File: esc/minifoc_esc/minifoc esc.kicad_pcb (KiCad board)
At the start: 4 copper layers, 31.6 x 23.8 mm, 47 parts, among them J2 Conn_01x03, J4 USB_C_Receptacle_USB2.0_16P, SW1 RESET, SW2 BOOT, U1 DRV8316CRRGFR, U2 RP2040, U3 W25Q64JVXGIQ TR, Y1 12Mhz

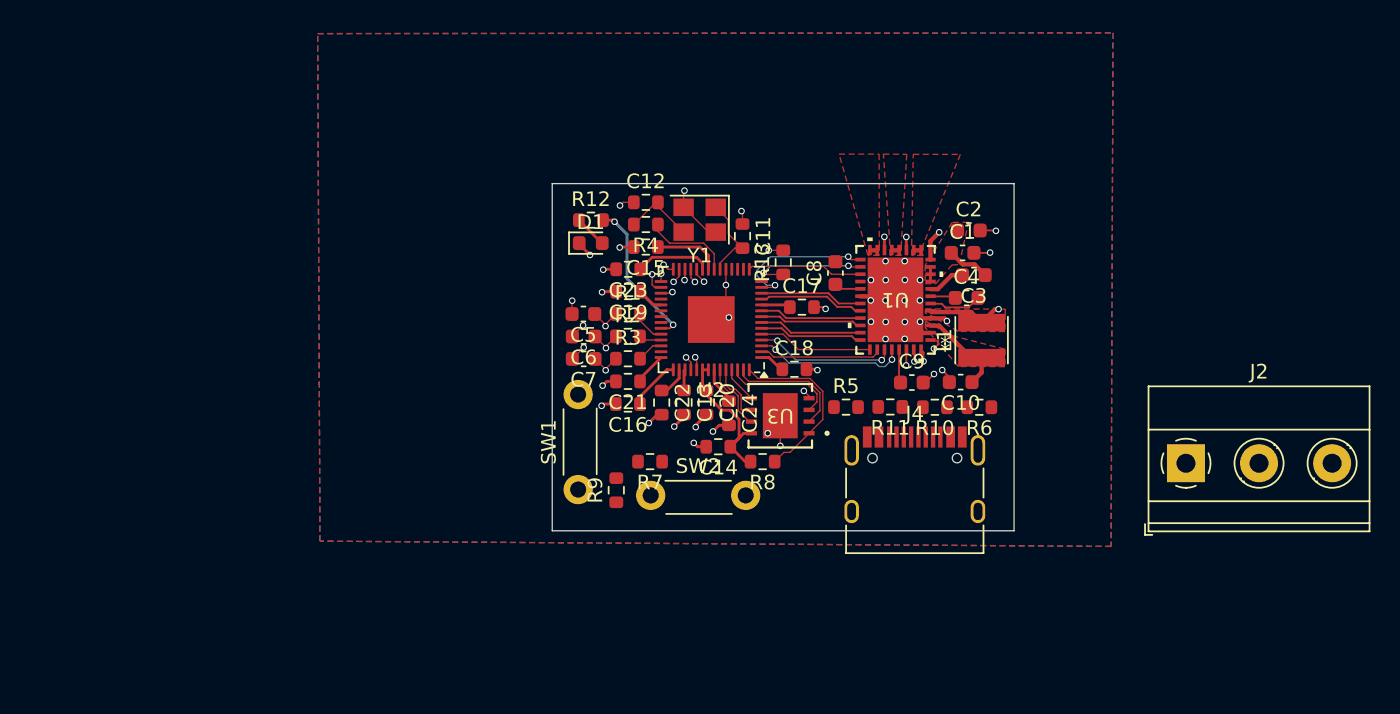
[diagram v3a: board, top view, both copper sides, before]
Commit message: Feat[minifoc_esc]: draft PCB
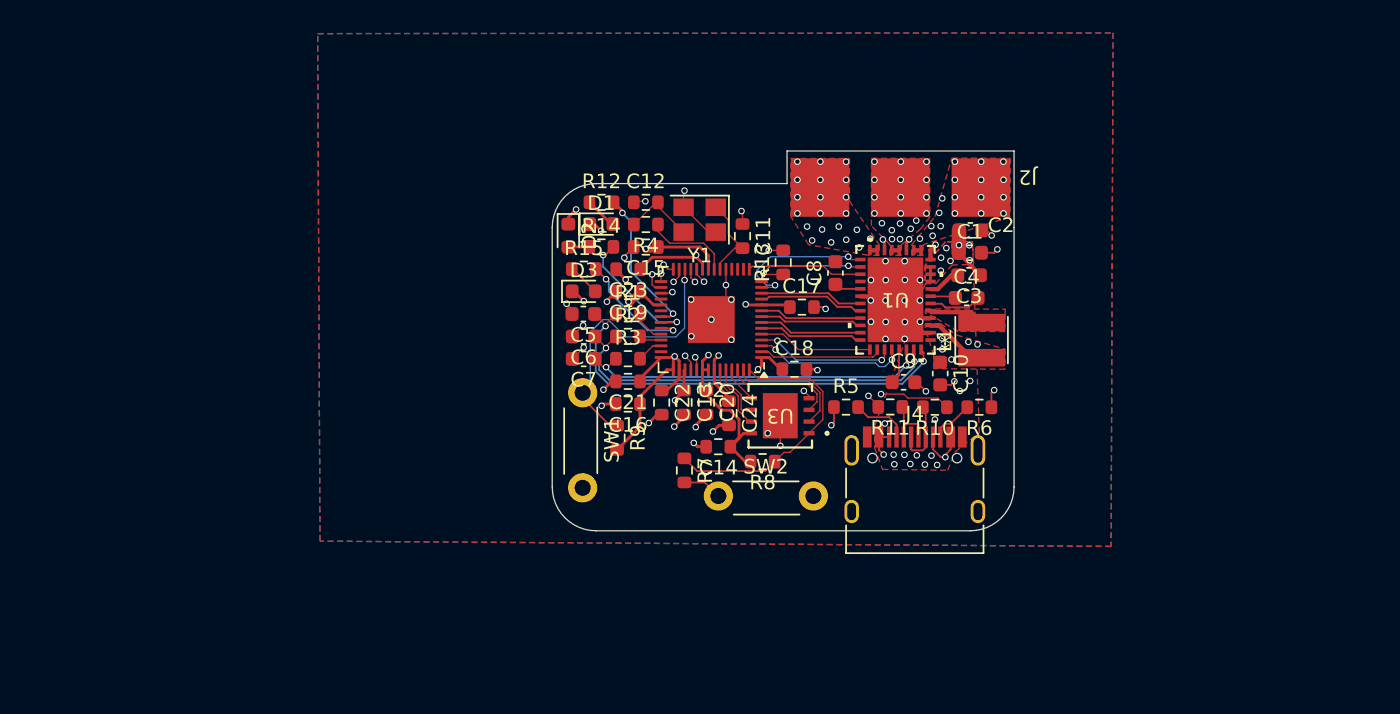
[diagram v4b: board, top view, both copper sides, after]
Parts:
- added D2: LED_Small, LED_SMD:LED_0603_1608Metric, F.Cu at (144.3, 104.0)
- added D3: LED_Small, LED_SMD:LED_0603_1608Metric, F.Cu at (145.4, 107.8)
- added R14: 2.7k, Resistor_SMD:R_0603_1608Metric, F.Cu at (146.6, 104.8)
- added R15: 2.7k, Resistor_SMD:R_0603_1608Metric, F.Cu at (145.4, 106.3)
- J2: footprint TerminalBlock_Phoenix:TerminalBlock_Phoenix_MKDS-1,5-3_1x03_P5.00mm_Horizontal -> DRV8316C:ESC
- moved J2 28.6 mm to (167.0, 98.7), turned to 180 degrees
- moved SW1 6.63 mm to (145.3, 114.8), turned to -90 degrees
- moved SW2 4.63 mm to (154.6, 121.8)
- moved R9 3.59 mm to (147.6, 117.8), turned to -90 degrees
- moved R7 2.43 mm to (152.2, 120.1), turned to -90 degrees
- moved C10 1.52 mm to (169.7, 113.5), turned to -90 degrees
- moved D1 1.49 mm to (146.6, 103.2)
- moved R12 1.42 mm to (146.6, 101.7)
- moved C9 0.57 mm to (167.2, 114.0)
- moved C1 0.51 mm to (171.8, 105.2)
- moved C3 0.33 mm to (171.7, 106.7)
- moved C2 0.10 mm to (171.8, 103.7)
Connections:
- J4 pad A4: /RP2040/VBUS -> VCC
- J4 pad A8: unconnected-(J4-SBU1-PadA8) -> VCC
- J4 pad A9: /RP2040/VBUS -> VCC
- J4 pad B4: /RP2040/VBUS -> VCC
- J4 pad B8: unconnected-(J4-SBU2-PadB8) -> VCC
- J4 pad B9: /RP2040/VBUS -> VCC
- R1 pad 2: /SOA -> /RP2040/SA
- R12 pad 2: /RP2040/LED -> /RP2040/LED3
- R2 pad 2: /SOB -> /RP2040/SB
- R3 pad 2: /SOC -> /RP2040/SC
- U2 pad 35: unconnected-(U2-GPIO23-Pad35) -> /RP2040/LED3
- U2 pad 36: unconnected-(U2-GPIO24-Pad36) -> /RP2040/LED2
- U2 pad 37: /RP2040/LED -> /RP2040/LED1
- U2 pad 38: /SOA -> /RP2040/SA
- U2 pad 39: /SOB -> /RP2040/SB
- U2 pad 40: /SOC -> /RP2040/SC
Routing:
- net /FB_BK: track 35.8 -> 88.6 mm, vias 1 -> 12
- net /SOA: track 5.42 -> 30.1 mm
- net /SOB: track 4.54 -> 27.3 mm
- net Net-(U2-USB_DP): track 0.90 -> 20.0 mm, vias 1 -> 2
- net /SOC: track 5.04 -> 24.1 mm
- net /RP2040/RUN: track 0.75 -> 19.4 mm
- net /RP2040/+1.1V: track 9.18 -> 27.6 mm, vias 0 -> 3
- net Net-(U2-USB_DM): track 0.98 -> 16.2 mm, vias 1 -> 2
- net /RP2040/LED: track 10.5 -> 0.00 mm, vias 2 -> 0
- net /RP2040/LED3: track 0.00 -> 10.2 mm, vias 0 -> 2
- net /RP2040/LED2: track 0.00 -> 9.43 mm, vias 0 -> 2
- net /RP2040/LED1: track 0.00 -> 8.29 mm, vias 0 -> 2
- net /RP2040/QSPI_CS: track 12.1 -> 18.9 mm
- net VCC: track 3.95 -> 10.2 mm, vias 0 -> 21
- net /RP2040/USB_P: track 0.00 -> 4.79 mm
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- added copper zone on In2.Cu, net /FB_BK
- added copper zone on In2.Cu, net OUTA
- added copper zone on In2.Cu, net OUTB
- added copper zone on In2.Cu, net OUTC
- added copper zone on In1.Cu, net VCC
- added copper zone on In2.Cu, net VCC
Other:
- board size 31.6 x 23.8 mm -> 31.6 x 26 mm
- board text added: "SWD"
- board text added: "TP"
- board text added: "Test points, swd, uart, pwm, smaller buttons (bottom left), reduce width, USBC recept. type impedance match usb? isolate agnd-pgnd-dgnd vcc route check sense lp filter"
- board text removed: "EDGE_CONN to esccarrier UART PHASES VCC GND"
- board text removed: "Test points, debugging interfaces?"

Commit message: Feat[minifoc_esc]: v1 final board design
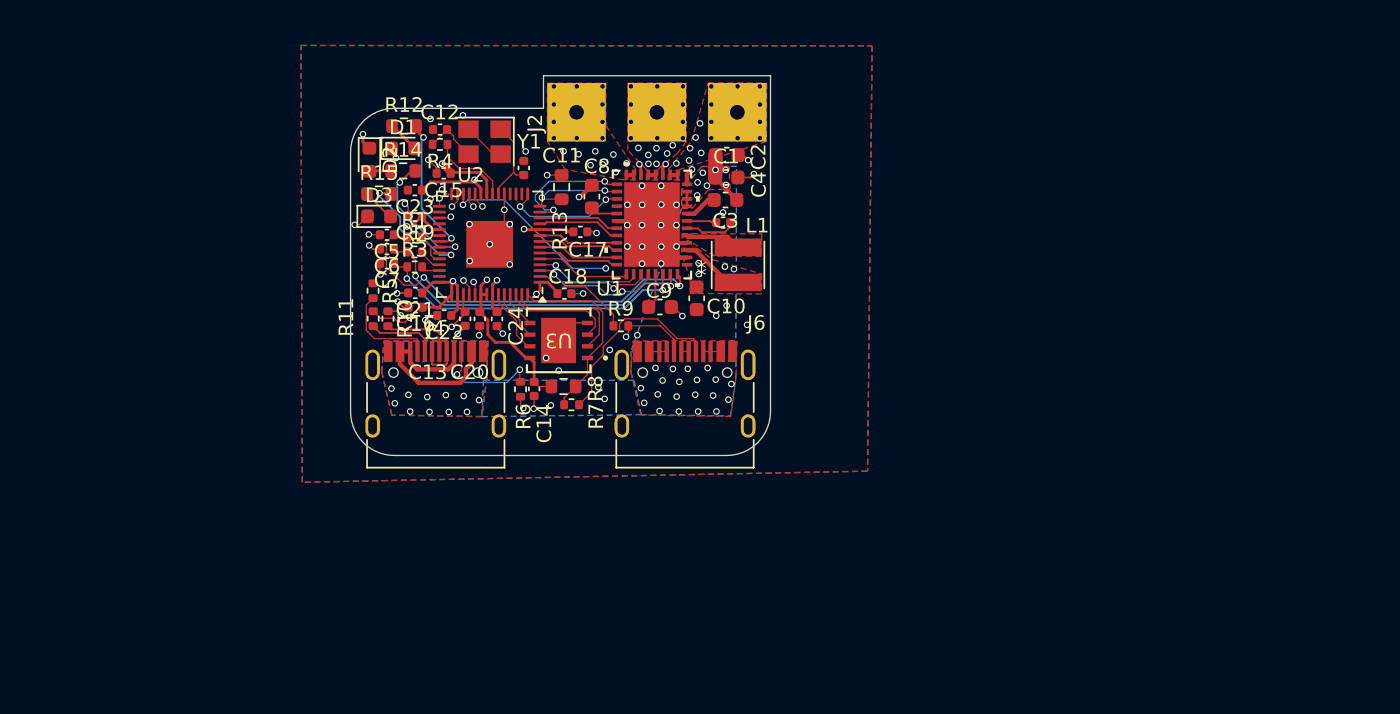
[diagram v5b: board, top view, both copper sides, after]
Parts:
- removed SW1: RESET, SLIM_Switch:SW_PUSH_6mm_SLIM
- removed SW2: BOOT, SLIM_Switch:SW_PUSH_6mm_SLIM
- added J6: USB_C_Receptacle_USB2.0_16P, Connector_USB:USB_C_Receptacle_HRO_TYPE-C-31-M-12, F.Cu at (152.3, 116.0)
- C11, C12, C13, C14, C15, C16, C17, C18, C19, C20, C21, C22, C23, C24: footprint Resistor_SMD:R_0603_1608Metric -> Capacitor_SMD:C_0402_1005Metric
- C4, C5, C6, C7: footprint Capacitor_SMD:C_0603_1608Metric -> Capacitor_SMD:C_0402_1005Metric
- R1, R10, R11, R2, R3, R4, R5, R6, R7, R9: footprint Resistor_SMD:R_0603_1608Metric -> Resistor_SMD:R_0402_1005Metric
- moved R10 37.9 mm to (132.0, 109.7), turned to -90 degrees
- moved R11 35.9 mm to (130.9, 109.7), turned to 90 degrees
- moved R5 33.3 mm to (130.9, 107.8), turned to -90 degrees
- moved J4 33.3 mm to (135.2, 116.0)
- moved R6 31.4 mm to (141.0, 114.5), turned to 90 degrees
- moved C8 17.5 mm to (145.9, 101.3)
- moved C4 17.4 mm to (154.9, 103.1)
- moved C2 17.4 mm to (155.1, 98.5)
- moved C3 17.4 mm to (155.1, 101.6)
- moved J2 17.4 mm to (150.4, 93.5)
- moved L1 17.4 mm to (155.9, 106.0)
- moved C1 17.4 mm to (155.1, 100.0)
- moved C10 17.4 mm to (153.1, 108.3)
- moved C9 17.4 mm to (150.6, 108.9)
- moved U1 17.4 mm to (150.0, 103.3)
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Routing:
- net VCC: track 10.2 -> 21.2 mm, vias 21 -> 44
- net /RP2040/USB_BOOT: track 2.71 -> 13.5 mm
- net GND: track 49.7 -> 39.4 mm
- net Net-(U2-USB_DP): track 20.0 -> 11.5 mm
- net /RP2040/QSPI_CS: track 18.9 -> 13.1 mm
- net /SOB: track 27.3 -> 22.8 mm
- net Net-(J4-CC2): track 3.04 -> 7.42 mm, vias 0 -> 2
- net /RP2040/RUN: track 19.4 -> 23.3 mm, vias 1 -> 3
- net Net-(U2-USB_DM): track 16.2 -> 12.4 mm
- net /SOA: track 30.1 -> 26.6 mm
- net /FB_BK: track 88.6 -> 85.4 mm, vias 12 -> 11
- net /RP2040/USB_P: track 4.79 -> 7.91 mm
- net Net-(J4-CC1): track 3.97 -> 6.98 mm
- net /RP2040/USB_N: track 4.76 -> 7.42 mm
- net /SOC: track 24.1 -> 21.7 mm
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- added copper zone on B.Cu, net VCC
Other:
- board size 31.6 x 26 mm -> 28.7 x 26 mm
- board text added: "isolate agnd-pgnd-dgnd"
- board text removed: "Test points, swd, uart, pwm, smaller buttons (bottom left), reduce width, USBC recept. type impedance match usb? isolate agnd-pgnd-dgnd vcc route check sense lp filter"
